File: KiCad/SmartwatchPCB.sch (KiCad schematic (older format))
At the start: 34 parts, among them IC1 ATSAML22G18A-MUT

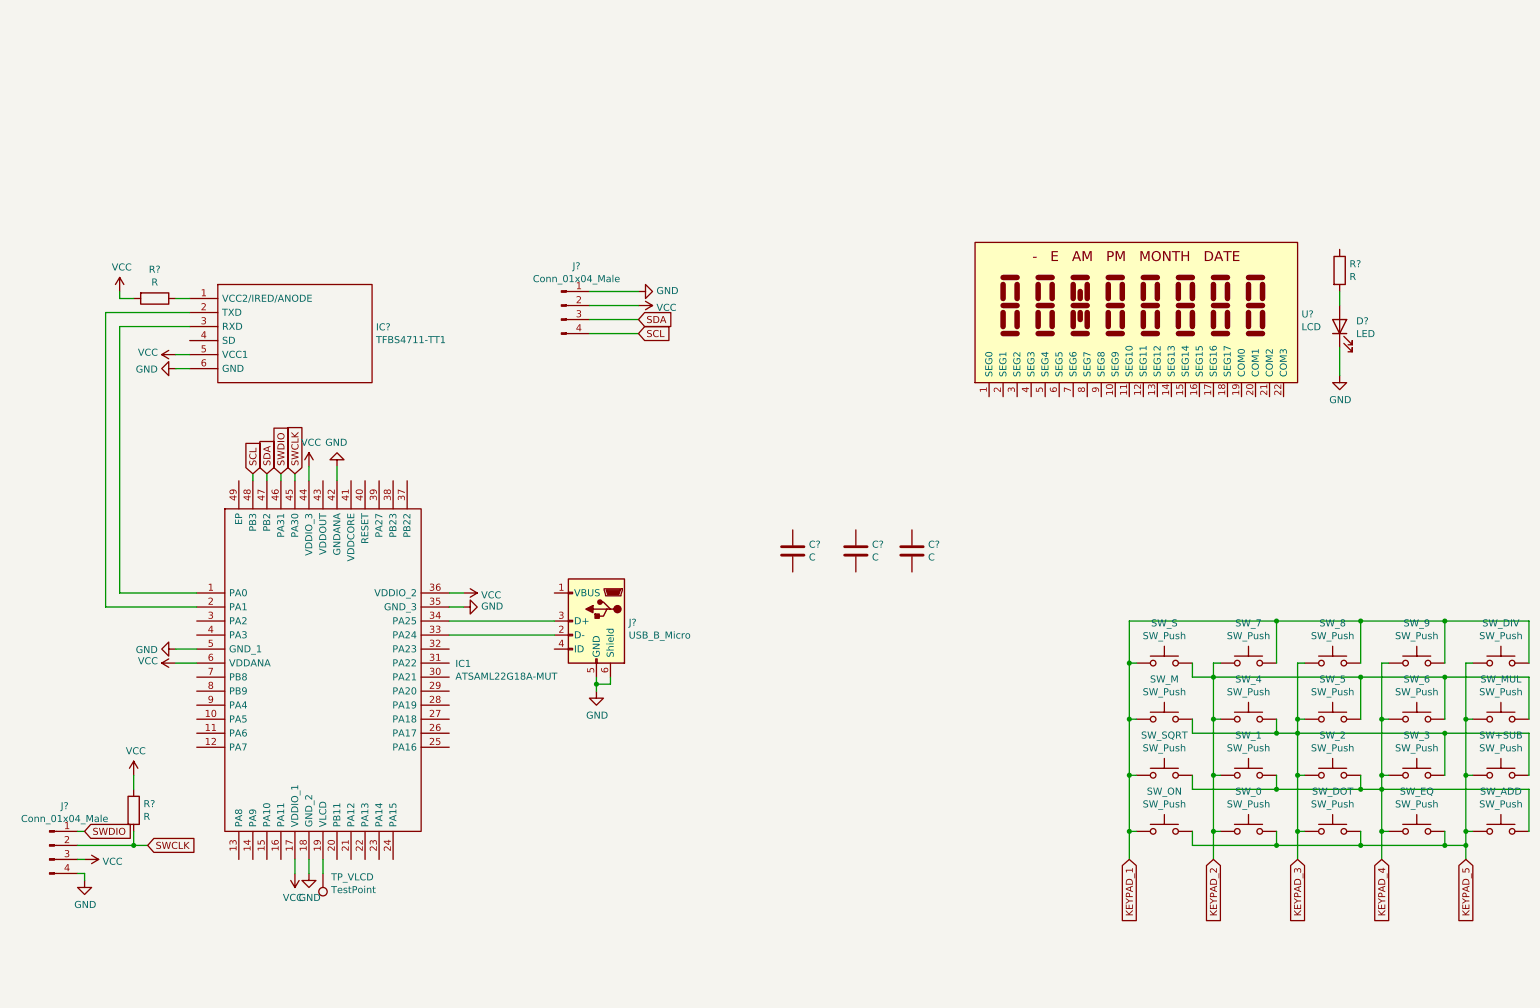
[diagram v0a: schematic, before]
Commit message: added button and lcd parts and sprinkled them
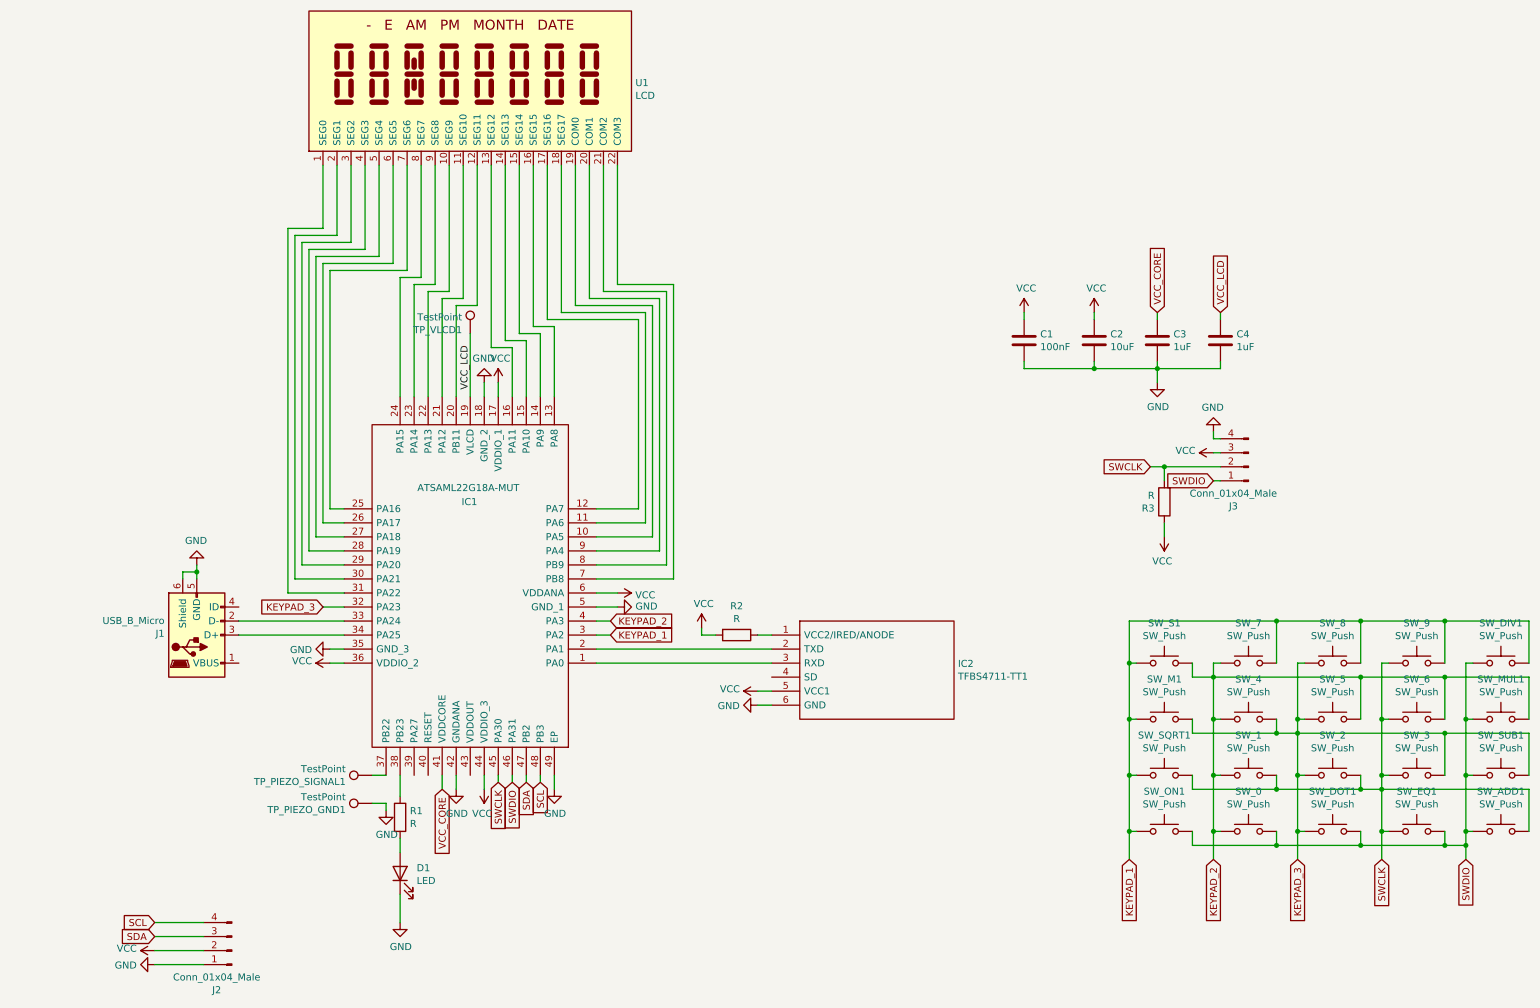
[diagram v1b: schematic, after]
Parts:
- added C4: 1uF, Capacitor_SMD:C_0603_1608Metric, symbol Device:C
- added TP_PIEZO_GND1, TP_PIEZO_SIGNAL1: TestPoint, TestPoint:TestPoint_Pad_D1.5mm, symbol Connector:TestPoint
- C1: renamed from C?; value C -> 100nF; footprint (none) -> Capacitor_SMD:C_0603_1608Metric
- C2: renamed from C?; value C -> 10uF; footprint (none) -> Capacitor_SMD:C_0603_1608Metric
- C3: renamed from C?; value C -> 1uF; footprint (none) -> Capacitor_SMD:C_0603_1608Metric
- D1: renamed from D?; footprint (none) -> LED_SMD:LED_0603_1608Metric_Castellated
- IC2: renamed from IC?; footprint TFBS4711TT1 -> TFBS4711-TT1:TFBS4711TT1
- J1: renamed from J?; footprint (none) -> Connector_USB:USB_Micro-B_Wuerth_629105150521_CircularHoles
- J2, J3: renamed from J?; footprint (none) -> Connector_PinHeader_1.27mm:PinHeader_1x04_P1.27mm_Vertical
- R1, R2, R3: renamed from R?; footprint (none) -> Resistor_SMD:R_0603_1608Metric
- SW_0, SW_1, SW_2, SW_3, SW_4, SW_5, SW_6, SW_7, SW_8, SW_9: footprint (none) -> SmartwatchPCB:button
- SW_ADD1: renamed from SW_ADD; footprint (none) -> SmartwatchPCB:button
- SW_DIV1: renamed from SW_DIV; footprint (none) -> SmartwatchPCB:button
- SW_DOT1: renamed from SW_DOT; footprint (none) -> SmartwatchPCB:button
- SW_EQ1: renamed from SW_EQ; footprint (none) -> SmartwatchPCB:button
- SW_M1: renamed from SW_M; footprint (none) -> SmartwatchPCB:button
- SW_MUL1: renamed from SW_MUL; footprint (none) -> SmartwatchPCB:button
- SW_ON1: renamed from SW_ON; footprint (none) -> SmartwatchPCB:button
- SW_S1: renamed from SW_S; footprint (none) -> SmartwatchPCB:button
- SW_SQRT1: renamed from SW_SQRT; footprint (none) -> SmartwatchPCB:button
- SW_SUB1: renamed from SW+SUB; footprint (none) -> SmartwatchPCB:button
- TP_VLCD1: renamed from TP_VLCD; footprint (none) -> TestPoint:TestPoint_Pad_D1.5mm
- U1: renamed from U?; footprint (none) -> SmartwatchPCB:display
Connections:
- net KEYPAD_4 is gone; now on net SWCLK: SW_1.2, SW_2.2, SW_3.1, SW_6.1, SW_9.1, SW_ADD1.2, SW_EQ1.1, SW_SQRT1.2
- net KEYPAD_5 is gone; now on net SWDIO: SW_0.2, SW_ADD1.1, SW_DIV1.1, SW_DOT1.2, SW_EQ1.2, SW_MUL1.1, SW_ON1.2, SW_SUB1.1
- net GND: now also C1.2, C2.2, C3.2, IC1.49 (EP), C4.2, TP_PIEZO_GND1.1
- net KEYPAD_1: now also IC1.3 (PA2)
- net KEYPAD_2: now also IC1.4 (PA3)
- net KEYPAD_3: now also IC1.32 (PA23)
- net VCC: now also C1.1, C2.1
- net at IC1.10 (PA5): now also U1.19 (COM0)
- net at IC1.11 (PA6): now also U1.18 (SEG17)
- net at IC1.12 (PA7): now also U1.17 (SEG16)
- net at IC1.13 (PA8): now also U1.16 (SEG15)
- net at IC1.14 (PA9): now also U1.15 (SEG14)
- net at IC1.15 (PA10): now also U1.14 (SEG13)
- net at IC1.16 (PA11): now also U1.13 (SEG12)
- net VCC_LCD: now reaches IC1.19 (VLCD), TP_VLCD1.1
- net VCC_LCD: now also C4.1
- net at IC1.20 (PB11): now also U1.12 (SEG11)
- net at IC1.21 (PA12): now also U1.11 (SEG10)
- net at IC1.22 (PA13): now also U1.10 (SEG9)
- net at IC1.23 (PA14): now also U1.9 (SEG8)
- net at IC1.24 (PA15): now also U1.8 (SEG7)
- net at IC1.25 (PA16): now also U1.7 (SEG6)
- net at IC1.26 (PA17): now also U1.6 (SEG5)
- net at IC1.27 (PA18): now also U1.5 (SEG4)
- net at IC1.28 (PA19): now also U1.4 (SEG3)
- net at IC1.29 (PA20): now also U1.3 (SEG2)
- net at IC1.30 (PA21): now also U1.2 (SEG1)
- net at IC1.31 (PA22): now also U1.1 (SEG0)
- net at IC1.37 (PB22): now also TP_PIEZO_SIGNAL1.1
- net at IC1.38 (PB23): now also R1.1
- net VCC_CORE: now reaches IC1.41 (VDDCORE)
- net VCC_CORE: now also C3.1
- net at IC1.7 (PB8): now also U1.22 (COM3)
- net at IC1.8 (PB9): now also U1.21 (COM2)
- net at IC1.9 (PA4): now also U1.20 (COM1)
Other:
- moved on the sheet: C1, C2, C3, D1, IC1, IC2, J1, J2, J3, R1, R2, R3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

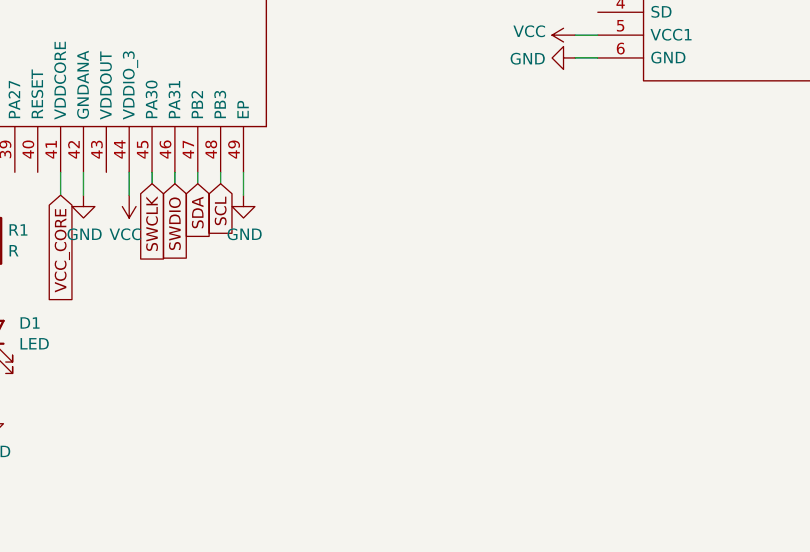
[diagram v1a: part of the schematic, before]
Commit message: more routing and footprint updates
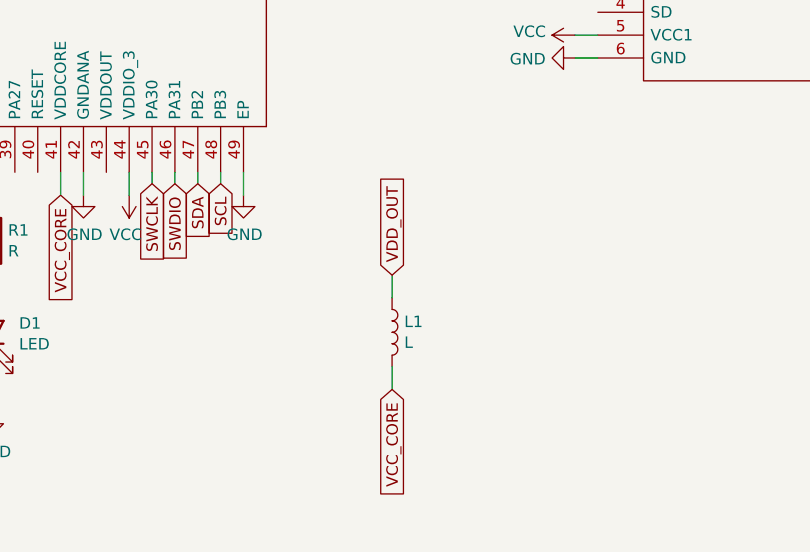
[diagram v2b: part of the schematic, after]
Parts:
- added L1: L, Inductor_SMD:L_0603_1608Metric, symbol Device:L
- J2: footprint Connector_PinHeader_1.27mm:PinHeader_1x04_P1.27mm_Vertical -> Connector_JST:JST_SH_SM04B-SRSS-TB_1x04-1MP_P1.00mm_Horizontal
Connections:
- net VCC_CORE: now also L1.2
- new net VDD_OUT: L1.1
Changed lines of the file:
@@
 F 0 "J2" H 1908 6881 50  0000 C CNN
 F 1 "Conn_01x04_Male" H 1908 6790 50  0000 C CNN
-F 2 "Connector_PinHeader_1.27mm:PinHeader_1x04_P1.27mm_Vertical" H 1800 6600 50  0001 C CNN
+F 2 "Connector_JST:JST_SH_SM04B-SRSS-TB_1x04-1MP_P1.00mm_Horizontal" H 1800 6600 50  0001 C CNN
 F 3 "~" H 1800 6600 50  0001 C CNN
 	1    1800 6600
@@
 Wire Wire Line
 	4100 5350 4100 5450
+$Comp
+L Device:L L1
+U 1 1 610A74F7
+P 4750 6050
+F 0 "L1" H 4803 6096 50  0000 L CNN
+F 1 "L" H 4803 6005 50  0000 L CNN
+F 2 "Inductor_SMD:L_0603_1608Metric" H 4750 6050 50  0001 C CNN
+F 3 "~" H 4750 6050 50  0001 C CNN
+	1    4750 6050
+	1    0    0    -1
+$EndComp
+Text GLabel 4750 6300 3    50   Input ~ 0
+VCC_CORE
+Wire Wire Line
+	4750 6300 4750 6200
+Wire Wire Line
+	4750 5900 4750 5800
+Text GLabel 4750 5800 1    50   Input ~ 0
+VDD_OUT
 $EndSCHEMATC

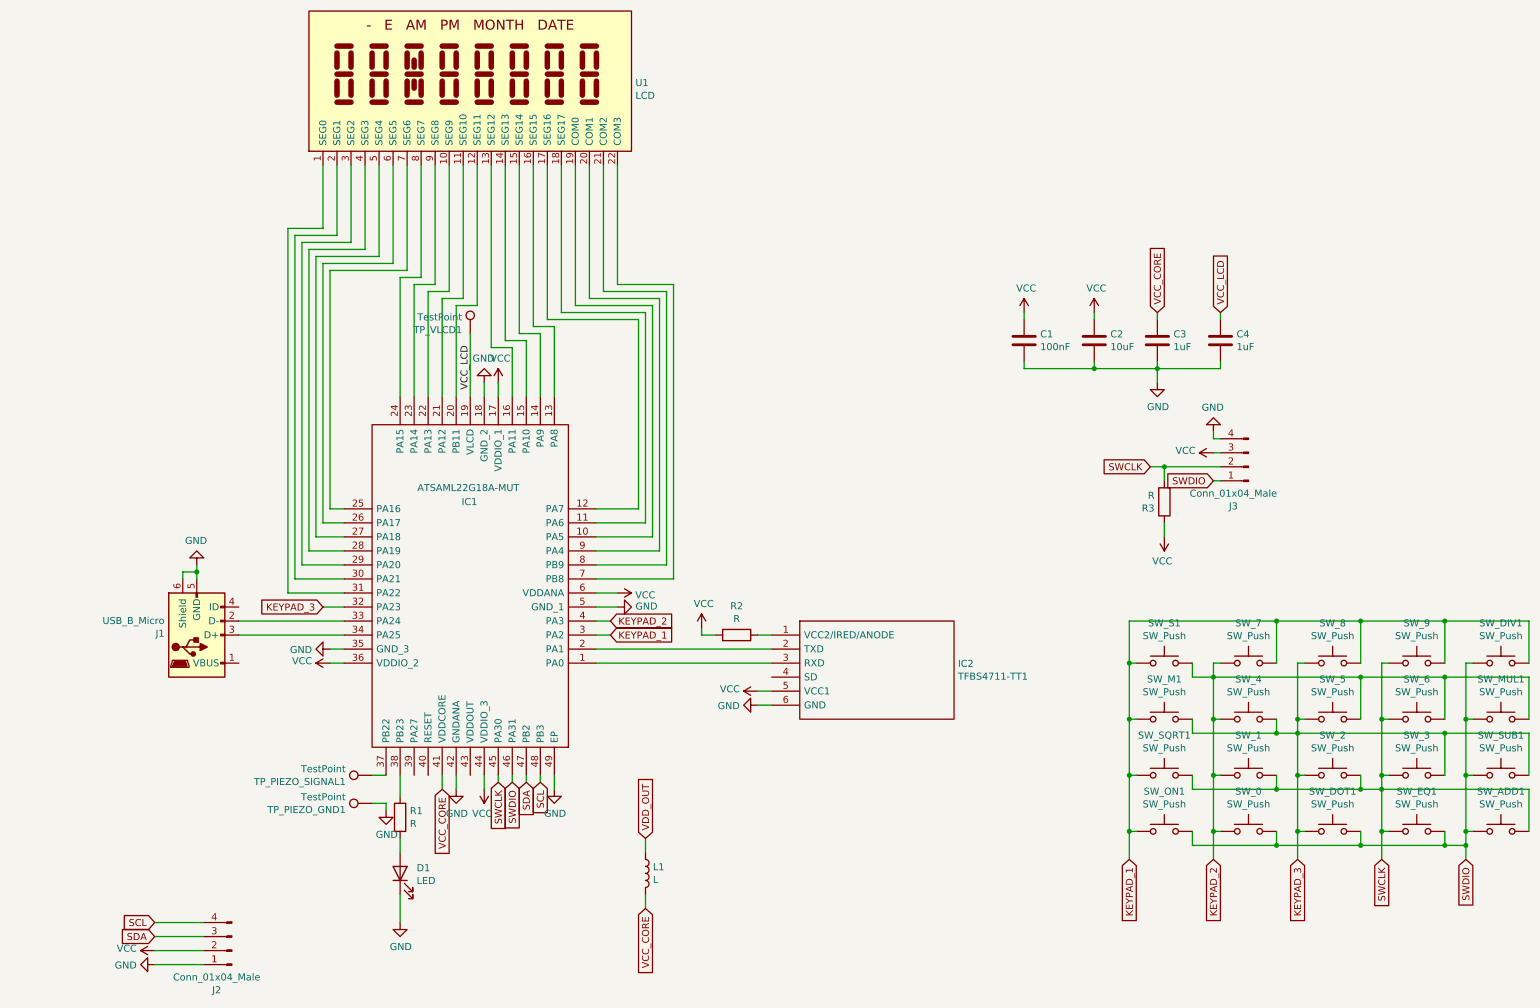
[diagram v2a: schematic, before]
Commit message: footprint and symbol libraries updated
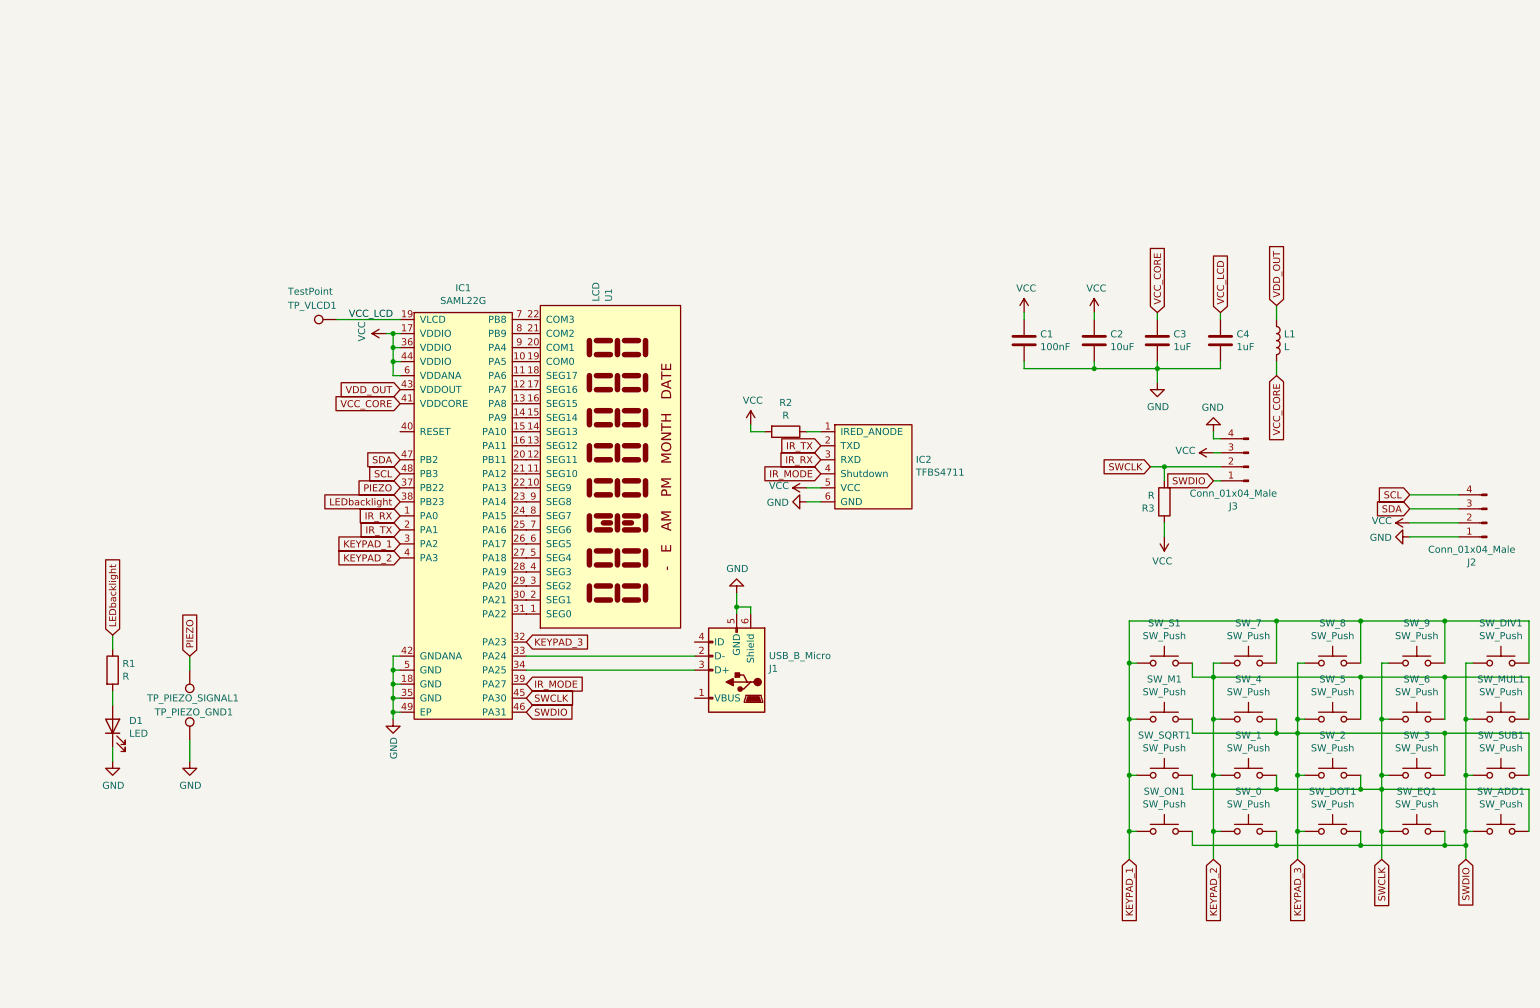
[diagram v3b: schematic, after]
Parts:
- removed IC1: ATSAML22G18A-MUT, ATSAML22G18A-MUT:QFN50P700X700X90-49N-D, symbol ATSAML22G18A-MUT:ATSAML22G18A-MUT
- removed IC2: TFBS4711-TT1, TFBS4711-TT1:TFBS4711TT1, symbol TFBS4711-TT1:TFBS4711-TT1
- added IC1: SAML22G, Package_DFN_QFN:QFN-48-1EP_7x7mm_P0.5mm_EP5.15x5.15mm, symbol SAML22G:SAML22G
- added IC2: TFBS4711, SmartwatchPCB:TFBS4711, symbol IR_transceiver:TFBS4711
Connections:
- net GND: now also IC1.18 (GND), IC1.35 (GND), IC1.42 (GNDANA), IC1.49 (EP), IC1.5 (GND), IC2.6 (GND)
- net KEYPAD_1: now also IC1.3 (PA2)
- net KEYPAD_2: now also IC1.4 (PA3)
- net KEYPAD_3: now also IC1.32 (PA23)
- net SCL: now also IC1.48 (PB3)
- net SDA: now also IC1.47 (PB2)
- net SWCLK: now also IC1.45 (PA30)
- net SWDIO: now also IC1.46 (PA31)
- net VCC: now also IC1.17 (VDDIO), IC1.36 (VDDIO), IC1.44 (VDDIO), IC1.6 (VDDANA), IC2.5 (VCC)
- net VCC_CORE: now also IC1.41 (VDDCORE)
- net VCC_LCD: now also IC1.19 (VLCD)
- net VDD_OUT: now also IC1.43 (VDDOUT)
- net at U1.19 (COM0): now also IC1.10 (PA5)
- net at U1.18 (SEG17): now also IC1.11 (PA6)
- net at U1.17 (SEG16): now also IC1.12 (PA7)
- net at U1.16 (SEG15): now also IC1.13 (PA8)
- net at U1.15 (SEG14): now also IC1.14 (PA9)
- net at U1.14 (SEG13): now also IC1.15 (PA10)
- net at U1.13 (SEG12): now also IC1.16 (PA11)
- net at U1.12 (SEG11): now also IC1.20 (PB11)
- net at U1.11 (SEG10): now also IC1.21 (PA12)
- net at U1.10 (SEG9): now also IC1.22 (PA13)
- net at U1.9 (SEG8): now also IC1.23 (PA14)
- net at U1.8 (SEG7): now also IC1.24 (PA15)
- net at U1.7 (SEG6): now also IC1.25 (PA16)
- net at U1.6 (SEG5): now also IC1.26 (PA17)
- net at U1.5 (SEG4): now also IC1.27 (PA18)
- net at U1.4 (SEG3): now also IC1.28 (PA19)
- net at U1.3 (SEG2): now also IC1.29 (PA20)
- net at U1.2 (SEG1): now also IC1.30 (PA21)
- net at U1.1 (SEG0): now also IC1.31 (PA22)
- net at J1.2 (D-): now also IC1.33 (PA24)
- net at J1.3 (D+): now also IC1.34 (PA25)
- net PIEZO: now reaches TP_PIEZO_SIGNAL1.1
- net PIEZO: now also IC1.37 (PB22)
- net LEDbacklight: now reaches R1.1
- net LEDbacklight: now also IC1.38 (PB23)
- net at U1.22 (COM3): now also IC1.7 (PB8)
- net at U1.21 (COM2): now also IC1.8 (PB9)
- net at U1.20 (COM1): now also IC1.9 (PA4)
- net at R2.1: now also IC2.1 (IRED_ANODE)
- new net IR_MODE: IC1.39 (PA27), IC2.4 (Shutdown)
- new net IR_RX: IC1.1 (PA0), IC2.3 (RXD)
- new net IR_TX: IC1.2 (PA1), IC2.2 (TXD)
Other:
- moved on the sheet: D1, J1, J2, L1, R1, R2, TP_PIEZO_GND1, TP_PIEZO_SIGNAL1, TP_VLCD1, U1
